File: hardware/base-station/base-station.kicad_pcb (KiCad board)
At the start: 4 copper layers, 30.3 x 90.5 mm, 123 parts, among them J2 USB4110GFA, J4 S3B-XH-A, J6 Conn_01x04, U1 W25Q64JVXGIQ TR, U12 MP2672AGD-0000-Z, U13 NTMD6N02R2G, U14 MAX17303G+, U15 479480001, U2 LM5157QRTERQ1, U22 TPS22918DBVR, U3 ESP32-S3RH2, U5 BQ21040DBVR, U9 TPS63021DSJR, Y1 ECS-.327-6-16R-TR, Y2 ECS-400-10-37B2-CKY-TR

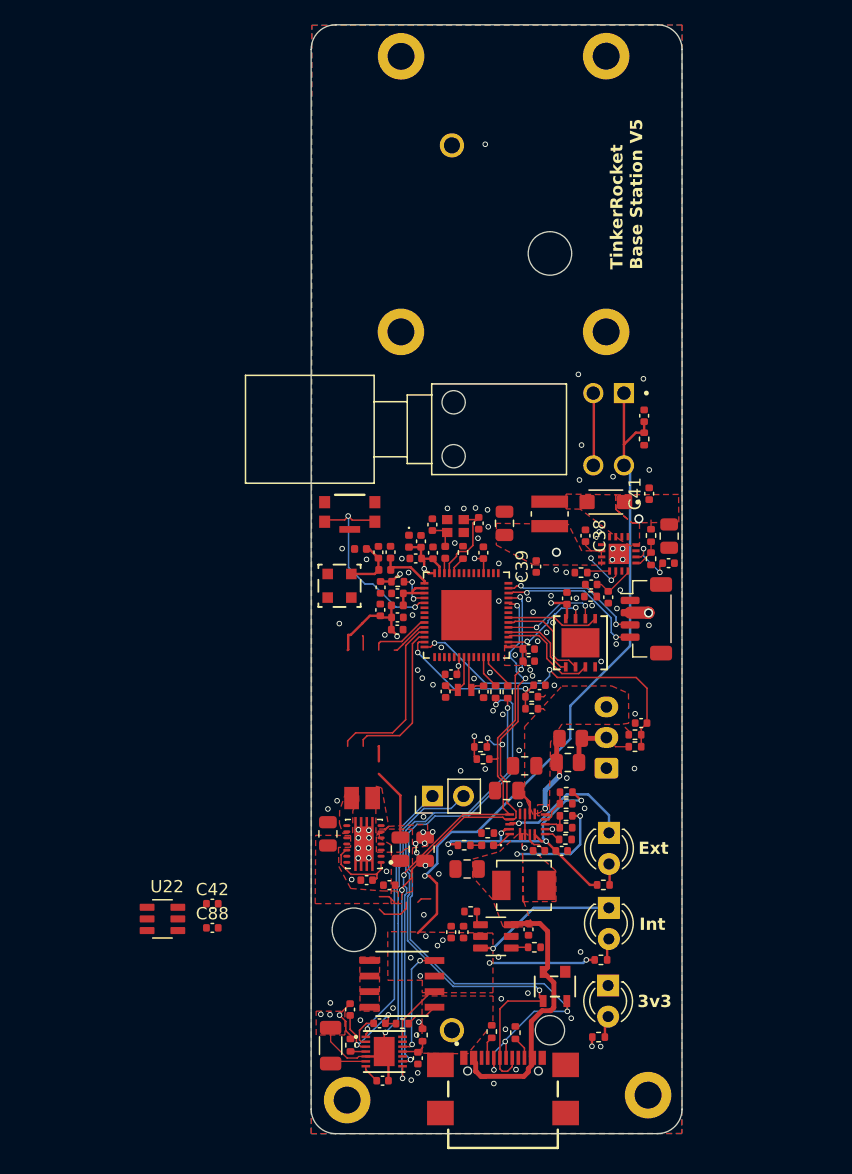
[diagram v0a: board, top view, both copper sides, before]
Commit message: hardware: battery protection, boost swap, and a capacitor voltage audit
Base station power chain, all verified against exported netlists:

- Protection: MAX17303G+ gauge/protector and its NTMD6N02R2G FET pair
  replaced by DW01A + 2x FS8205A. The MAX17303 had no firmware driver and
  the board never had a working coulomb counter, so state of charge already
  came from the voltage curve in bs_battery_soc.h; it now reads a 1M/1M
  divider on GPIO1. The FETs move from the positive rail to the negative
  one because the DW01A has no charge pump, so board ground is now P-,
  separated from the cell's B- by the FET stack. Two FS8205A in parallel
  put the 150 mV overcurrent trip at ~4.8-6.0 A instead of ~2.4-3.0 A.
  TH1 moves onto the BQ21040's TS pin, replacing a fixed 10k that had been
  defeating thermal charge cutoff.

- V_LORA retargeted 7.49 V -> 4.95 V and LM5157QRTERQ1 -> TPS61023DRLR.
  Nothing needed 7.4 V (everything downstream is 3.3 V behind the
  TPS62913), while an RFD868x-class radio is 5 V nominal with a 6 V
  absolute maximum, so the old rail put it permanently out of reach. Being
  synchronous and internally compensated also dropped D2, C35-C38 and R10.
  Inductor stays the fleet 2.2 uH: inside TI's 0.37-2.9 uH range and the
  only value meeting their ripple-under-40%-of-average guidance at load.

- Keystone 1043P holder -> MYOUNG BH-18650-A5BJ001-2D. Terminal pitch
  72.30 vs 72.22 mm, so the battery nets did not move; BT2 is rotated 180
  degrees because this part's positive end is mirrored.

Across all four boards:

- Every crystal was mis-loaded. 32.768 kHz parts saw ~9 pF against a 6 pF
  spec and the 40 MHz saw 12.5 pF against 10 pF, both pulling slow. Moved
  to Seiko SC-32S (12.5 pF) with 22 pF load caps, and the 40 MHz caps to
  18 pF. The tolerance being paid for had been swamped several times over.

- Capacitor voltage audit, new Min V rating column in the BOM. Three parts
  were operating outside their rating on 8.4 V rails: 47 uF and 100 u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
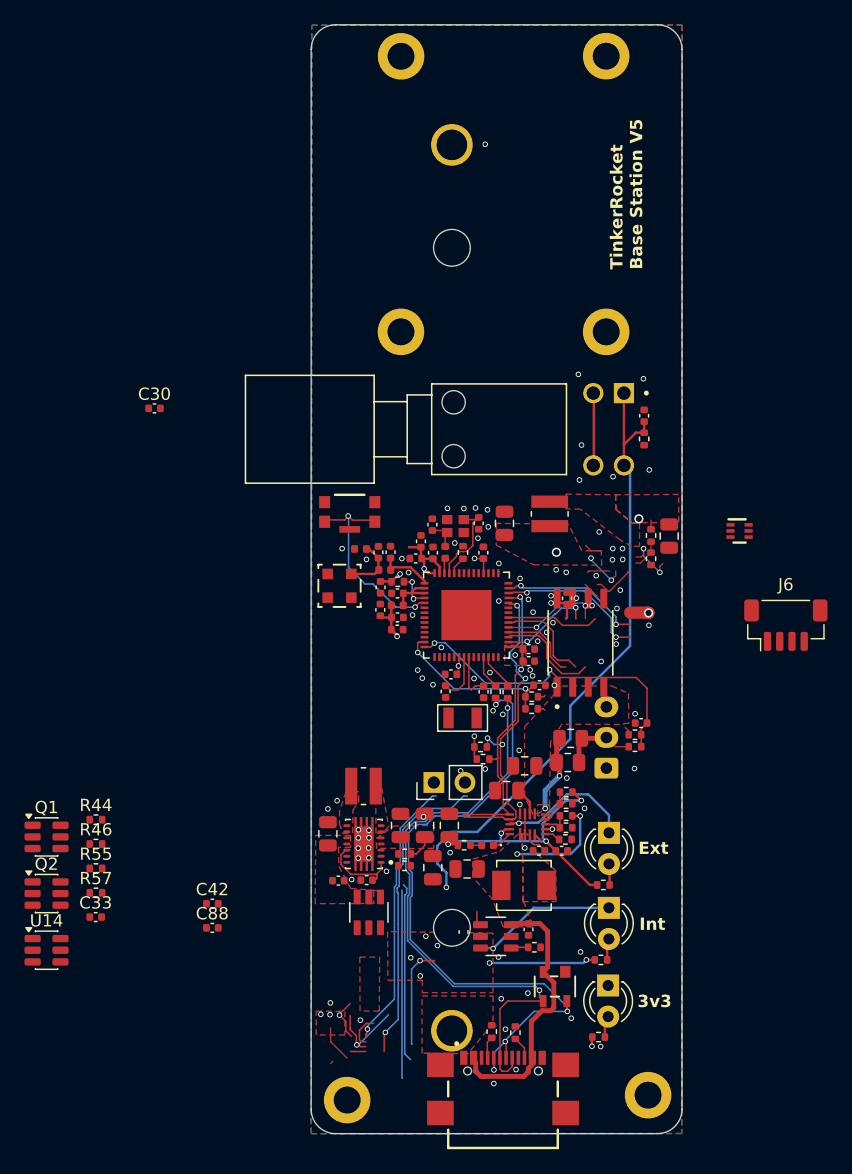
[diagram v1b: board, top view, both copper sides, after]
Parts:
- removed C20, C38: 1 uF, Capacitor_SMD:C_0402_1005Metric
- removed C31: 470 nF, Capacitor_SMD:C_0402_1005Metric
- removed C32, C39, C41: 100 nF, Capacitor_SMD:C_0402_1005Metric
- removed C35: 300 pF, Capacitor_SMD:C_0402_1005Metric
- removed C36: 15 nF, Capacitor_SMD:C_0402_1005Metric
- removed C37: 10 nF, Capacitor_SMD:C_0402_1005Metric
- removed D1: D_TVS, Diode_SMD:D_0402_1005Metric
- removed D2: SS24FL, Footprints:SODFL3617X108N
- removed L5: DFE201610E-1R0M=P2, Footprints:INDC2016X100N
- removed R10, R53: 10 k, Resistor_SMD:R_0402_1005Metric
- removed R18: 10 m, Resistor_SMD:R_1206_3216Metric
- removed the R40 at (61.8, 169.6)
- removed R56: 10, Resistor_SMD:R_0402_1005Metric
- removed R9: 442, Resistor_SMD:R_0402_1005Metric
- removed U13: NTMD6N02R2G, Footprints:SOIC8_4X5_ONS
- added C61: 22 uF, Capacitor_SMD:C_0805_2012Metric, F.Cu at (58.7, 169.0)
- added C62: 22 uF, Capacitor_SMD:C_0805_2012Metric, F.Cu at (57.3, 172.4)
- added L9: VLS3012CX-2R2M-1, Footprints:IND_VLS3012CX-2R2M-1, F.Cu at (51.7, 165.8)
- added Q1: FS8205A, Package_TO_SOT_SMD:SOT-23-6, F.Cu at (25.8, 169.9)
- added Q2: FS8205A, Package_TO_SOT_SMD:SOT-23-6, F.Cu at (25.8, 174.5)
- added R13: 1 M, Resistor_SMD:R_0402_1005Metric, F.Cu at (55.0, 171.3)
- added R16: 180 k, Resistor_SMD:R_0402_1005Metric, F.Cu at (55.0, 172.3)
- added R44: 1 M, Resistor_SMD:R_0402_1005Metric, F.Cu at (29.8, 168.5)
- added R46: 1 M, Resistor_SMD:R_0402_1005Metric, F.Cu at (29.8, 170.5)
- BT2: value 1043P -> BH-18650-A5BJ001-2D; footprint Footprints:BAT_1043P -> Footprints:BAT_BH-18650-A5BJ001-2D
- C2, C4: value 15 pF -> 22 pF
- C3, C6: value 22 pF -> 18 pF
- R11: value 100 k -> 732 k
- R12: value 15.4 k -> 100 k
- R57: value 1 k -> 2 k
- U1: value W25Q64JVXGIQ TR -> W25Q128JVSIQ; footprint Footprints:DFN_XGIQ TR_WIN -> Footprints:SOIC-8_W25Q128JVSIQ
- U14: value MAX17303G+ -> DW01A; footprint Footprints:21-0137I_T1433-2_MXM -> Package_TO_SOT_SMD:SOT-23-6
- U2: value LM5157QRTERQ1 -> TPS61023DRLR; footprint Footprints:RTE0016K -> Footprints:DRL0006A
- U9: value TPS63021DSJR -> TPS63020DSJR
- Y1: value ECS-.327-6-16R-TR -> SC-32S-32.768kHz-12.5pF; footprint Footprints:XTAL_ECS-.327-6-16R-TR -> Footprints:XTAL_SC-32S_3215
- moved C30 57.2 mm to (34.6, 134.9), turned to 0 degrees
- moved R55 29.9 mm to (29.8, 172.5), turned to 0 degrees
- moved U14 28.8 mm to (25.8, 179.2)
- moved R57 24.2 mm to (29.8, 174.5), turned to 0 degrees
- moved C33 22.1 mm to (29.8, 176.5), turned to 0 degrees
- moved U22 16.9 mm to (52.1, 176.1), turned to 90 degrees
- moved J6 11.4 mm to (86.1, 152.6), turned to 0 degrees
- moved U2 10.0 mm to (82.4, 145.0)
- moved C23 4.18 mm to (49.6, 173.5), turned to 0 degrees
- moved Y1 2.29 mm to (59.8, 160.2)
- moved C60 1.93 mm to (56.7, 169.0), turned to 90 degrees
- moved C58 1.93 mm to (54.7, 169.0), turned to 90 degrees
- moved TH1 1.12 mm to (57.4, 165.5)
- turned BT2 to 90 degrees
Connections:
- net Vcc renamed CHG_VCC
- BT2 pad N: Net-(U14-CSP) -> /Battery/B-
- BT2 pad P: Net-(U13-SOURCE1) -> VCC
- C30 pad 1: Net-(U14-PCKP) -> Volt_Read
- C33 pad 1: Net-(U14-BATT) -> Net-(U14-VCC)
- C33 pad 2: Net-(U14-CSP) -> /Battery/B-
- L8 pad 2: Net-(D2-PadA) -> Net-(U2-SW)
- R55 pad 2: Net-(U14-PCKP) -> Net-(U14-VCC)
- R57 pad 1: Net-(U14-CSP) -> Net-(U14-VM)
- R57 pad 2: Net-(U14-PFAIL) -> GND
- TH1 pad 1: Net-(U14-TH) -> Net-(U5-TS)
- TH1 pad 2: Net-(U14-CSP) -> GND
- U14 pad 1: Net-(U14-TH) -> Net-(Q1-G1)
- U14 pad 2: Net-(U14-CP) -> Net-(U14-VM)
- U14 pad 3: Net-(U14-BATT) -> Net-(Q1-G2)
- U14 pad 4: Net-(U14-PFAIL) -> unconnected-(U14-TD-Pad4)
- U14 pad 5: Net-(U14-CSP) -> Net-(U14-VCC)
- U14 pad 6: GND -> /Battery/B-
- U2 pad 1: GND -> Net-(U2-FB)
- U2 pad 2: Net-(U2-VCC) -> VCC
- U2 pad 4: unconnected-(U2-PGOOD-Pad4) -> GND
- U2 pad 5: Net-(U2-RT) -> Net-(U2-SW)
- U2 pad 6: VCC -> V_LORA
- U3 pad 38: SDA_SENS -> unconnected-(U3-GPIO33-Pad38)
- U3 pad 39: SCL_SENS -> unconnected-(U3-GPIO34-Pad39)
- U3 pad 6: unconnected-(U3-GPIO1-Pad6) -> Volt_Read
- U9 pad 3: +3V3 -> Net-(U9-FB)
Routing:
- net GND: track 4.33 -> 48.7 mm, vias 102 -> 95
- net Net-(U14-CSP): track 37.4 -> 0.00 mm, vias 4 -> 0
- net SDA_SENS: track 51.5 -> 27.2 mm, vias 6 -> 4
- net SCL_SENS: track 47.8 -> 24.7 mm, vias 4 -> 2
- net Net-(U14-TH): track 22.2 -> 0.00 mm, vias 1 -> 0
- net Net-(U5-TS): track 1.20 -> 23.4 mm, vias 0 -> 1
- net (no net): track 5.66 -> 27.3 mm, vias 0 -> 4
- net Net-(U9-FB): track 0.00 -> 14.6 mm
- net M_FLASH_CS: track 13.9 -> 0.00 mm
- net M_MISO: track 12.8 -> 0.00 mm
- net Net-(U13-GATE2): track 9.19 -> 0.00 mm, vias 2 -> 0
- net Net-(U14-BATT): track 8.72 -> 0.00 mm, vias 2 -> 0
- net +3V3: track 28.3 -> 19.9 mm, vias 10 -> 7
- net Net-(U22-ON): track 57.2 -> 52.1 mm
- net M_SCK: track 4.99 -> 0.00 mm
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- added copper zone on F.Cu, net (none)
- added copper zone on In2.Cu, net /Battery/B-
- added copper zone on F.Cu, net Net-(U2-SW)
- removed copper zone on F.Cu, net Net-(D2-PadA)
- removed copper zone on F.Cu, net Net-(U13-DRAIN1-Pad7)
- removed copper zone on F.Cu, net Net-(U13-SOURCE1)
- removed copper zone on F.Cu, net Net-(U14-CSP)
- removed copper zone on In2.Cu, net Net-(U14-CSP)

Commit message: hardware: place Q3 and bump C10 to 10 uF on the base-station
Places the third FS8205A whose schematic went in with the previous
commit, so the protection stack is now Q1/Q2/Q3 on the board as well as
on the sheet.

C10 goes 1 uF -> 10 uF. Changed in both esp32_p3.kicad_sch and the
layout, so schematic and board agree.

The battery sheet is rewired - +9 wires, +3 junctions, -5 labels - with
no change to its part set.

Layout otherwise: 38 parts repositioned, 24 track segments removed, 35
vias added, one zone removed.

Co-Authored-By: Claude Opus 5 <noreply@anthropic.com>
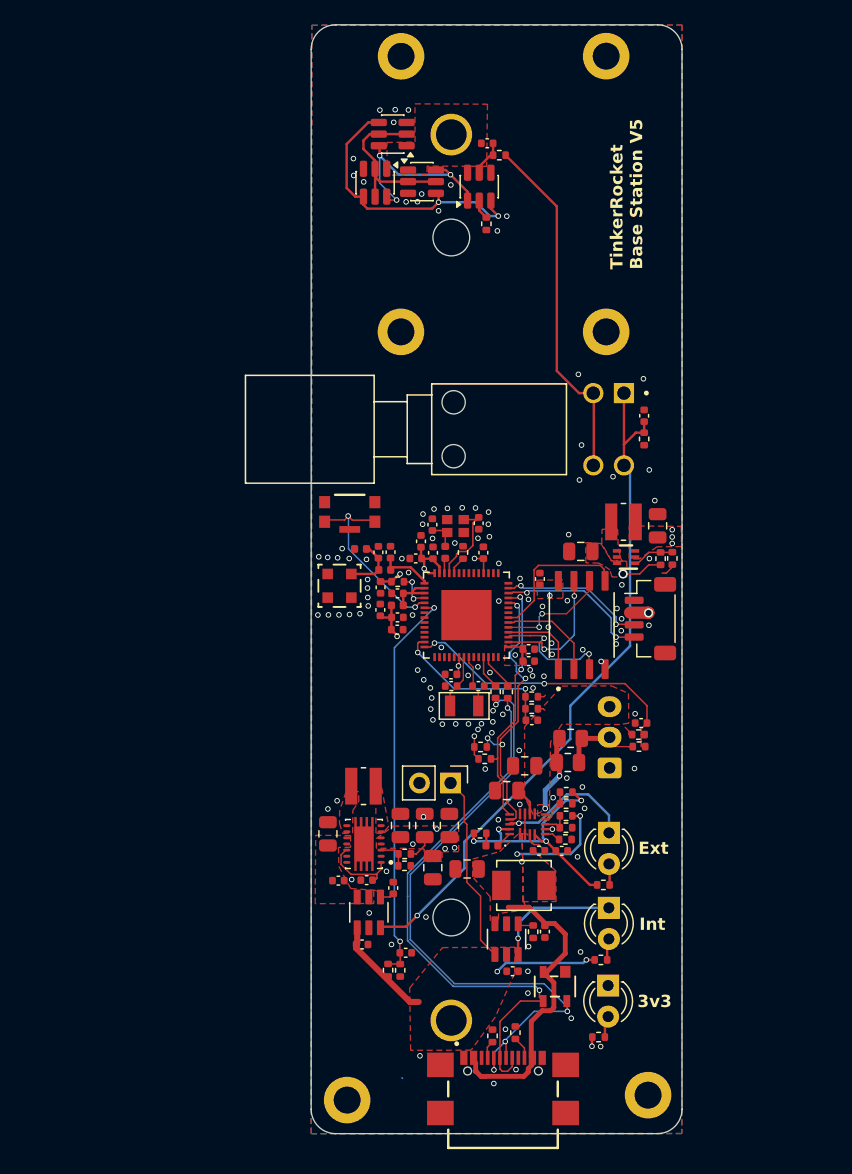
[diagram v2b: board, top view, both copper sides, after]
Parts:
- added Q3: FS8205A, Package_TO_SOT_SMD:SOT-23-6, F.Cu at (52.6, 116.5)
- C10: value 1 uF -> 10 uF
- R55: value 1 k -> 100
- moved U14 71.6 mm to (61.1, 116.8), turned to 90 degrees
- moved C33 70.8 mm to (61.8, 113.3), turned to 180 degrees
- moved Q2 68.1 mm to (54.1, 112.6), turned to 180 degrees
- moved R55 66.9 mm to (62.8, 114.3), turned to 180 degrees
- moved R57 63.2 mm to (61.7, 119.9), turned to -90 degrees
- moved Q1 61.6 mm to (56.4, 116.4)
- moved C30 48.9 mm to (55.1, 179.4)
- moved R46 26.9 mm to (54.7, 180.8), turned to -90 degrees
- moved R44 26.8 mm to (53.7, 180.8), turned to 90 degrees
- moved C88 15.1 mm to (54.1, 174.1), turned to 90 degrees
- moved C42 12.7 mm to (51.6, 178.7)
- moved C34 12.5 mm to (75.7, 144.5)
- moved J6 11.1 mm to (75.1, 152.1), turned to -90 degrees
- moved U2 9.51 mm to (73.1, 147.1), turned to 180 degrees
- moved C40 7.32 mm to (69.4, 146.6), turned to 180 degrees
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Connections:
- net Net-(Q1-D1/D2-Pad2) renamed /Battery/PROT_DRAIN
- U3 pad 38: unconnected-(U3-GPIO33-Pad38) -> SDA_SENS
- U3 pad 39: unconnected-(U3-GPIO34-Pad39) -> SCL_SENS
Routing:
- net GND: track 48.7 -> 2.69 mm, vias 95 -> 125
- net Volt_Read: track 0.00 -> 32.4 mm, vias 0 -> 2
- net (no net): track 27.3 -> 0.00 mm, vias 4 -> 0
- net Net-(Q1-G2): track 0.00 -> 23.4 mm, vias 0 -> 2
- net VCC: track 89.9 -> 112.5 mm, vias 8 -> 5
- net Net-(Q1-G1): track 0.00 -> 16.4 mm, vias 0 -> 3
- net /Battery/PROT_DRAIN: track 0.00 -> 14.5 mm
- net Net-(U9-FB): track 14.6 -> 2.66 mm
- net Net-(U5-TS): track 23.4 -> 15.5 mm, vias 1 -> 0
- net Net-(U22-ON): track 52.1 -> 57.1 mm
- net SDA_SENS: track 27.2 -> 23.4 mm
- net SCL_SENS: track 24.7 -> 20.9 mm
- net SPI_HD: track 7.67 -> 10.7 mm
- net Net-(U14-VCC): track 0.00 -> 3.02 mm
- net VBUS: track 30.4 -> 33.2 mm
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- added copper zone on F.Cu, net /Battery/B-
- removed copper zone on F.Cu, net (none)
- removed copper zone on In2.Cu, net /Battery/B-

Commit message: hardware: single-source each board's version through the title block
Every board hardcoded its marketing version inside a silkscreen gr_text
("LoRa V3", "Tinker\nRocket\nV9", ...), where it could drift from the git
tag with nothing to catch it.

The version token now lives in the PCB title block as (rev "V3") and the
silkscreen references ${REVISION}. KiCad resolves that at plot time,
including from kicad-cli, so the artwork is unchanged -- verified by
plotting F.SilkS + B.SilkS for all five boards before and after and
comparing stroke counts:

  lora-daughterboard      260 -> 260
  rocket-computer        1236 -> 1236
  base-station            687 -> 687
  gnss-sam10m8-18mm-hv    366 -> 366
  gnss-px1105r-...        353 -> 353

Four changed lines per board and nothing else. servo-adapter is untouched
-- it carries no version on silkscreen yet.

Co-Authored-By: Claude Opus 5 <noreply@anthropic.com>
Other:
- board text added: "TinkerRocket Base Station ${REVISION}"
- board text removed: "TinkerRocket Base Station V5"
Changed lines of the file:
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@@
 	)
 	(paper "A4")
+	(title_block
+		(rev "V5")
+	)
 	(layers
 		(0 "F.Cu" signal)
@@
 		)
 	)
-	(gr_text "TinkerRocket\nBase Station V5"
+	(gr_text "TinkerRocket\nBase Station ${REVISION}"
 		(at 74.54 123.61 90)
 		(layer "F.SilkS")

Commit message: hardware: declare filled+capped vias on the 6-layer boards; in-progress board edits
Two separate things, kept together because they land in the same board files.

1. Via protection, mine.  lora-daughterboard and rocket-computer both place
   vias in pads, and the fab fills those on 6-layer stackups -- but the board
   files still declared (filling no) (capping no), so nothing in the exported
   data said so.  Both now declare IPC-4761 Type VII (filled and capped),
   which is the process via-in-pad actually requires.  base-station is left at
   (filling no) (capping no): it is 4-layer and does not get the treatment.

2. In-progress layout work, the user's, carried along in the same files:

   rocket-computer  J7 removed (superseded by the J8 JST VH battery inlet);
                    C20/C22/C48/C49 crystal caps 18 pF -> 12 pF now reflected
                    in copper; 8 parts flipped side, 23 repositioned, routing
                    and via count adjusted to suit
   lora-daughterboard  routing and ground stitching (+8 vias, +10 segments)
   base-station     one via removed
   gnss-sam10m8-18mm-hv       C15 added; C11/C13 47 uF -> 22 uF
   gnss-px1105r-...-ext-ant   C16/R8/R9 added; C13/C14 47 uF -> 22 uF

The 47 -> 22 uF swap on both GNSS boards is already reflected in the
cross-board BOM: the 47 uF line is now rocket-computer only (1), and 22 uF
GNSS went 5 -> 8.

Co-Authored-By: Claude Opus 5 <noreply@anthropic.com>
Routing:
- net GND: vias 125 -> 124
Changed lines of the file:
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@@
 	)
 	(via
-		(at 56.57 168.28)
-		(size 0.45)
-		(drill 0.3)
-		(layers "F.Cu" "B.Cu")
-		(free yes)
-		(net "GND")
-	)
-	(via
 		(at 72.76 149.35)
 		(size 0.45)
@@
 	)
 	(segment
+		(start 51.67 113.08)
+		(end 52.19 112.56)
+		(width 0.2)
+		(layer "F.Cu")
+		(net "/Battery/PROT_DRAIN")
+	)
+	(segment
+		(start 54.37 112.56)
+		(end 55.195 112.56)
+		(width 0.2)
+		(layer "F.Cu")
+		(net "/Battery/PROT_DRAIN")
+	)
+	(segment
+		(start 52.62 114.727501)
+		(end 51.67 113.777501)
+		(width 0.2)
+		(layer "F.Cu")
+		(net "/Battery/PROT_DRAIN")
+	)
+	(segment
+		(start 53.007501 116.44)
+		(end 52.62 116.052499)
+		(width 0.2)
+		(layer "F.Cu")
+		(net "/Battery/PROT_DRAIN")
+	)
+	(segment
+		(start 54.37 112.56)
+		(end 52.92 112.56)
+		(width 0.2)
+		(layer "F.Cu")
+		(net "/Battery/PROT_DRAIN")
+	)
+	(segment
+		(start 52.62 115.39)
+		(end 52.62 114.727501)
+		(width 0.2)
+		(layer "F.Cu")
+		(net "/Battery/PROT_DRAIN")
+	)
+	(segment
+		(start 52.62 115.39)
+		(end 52.62 117.665)
+		(width 0.2)
+		(layer "F.Cu")
+		(net "/Battery/PROT_DRAIN")
+	)
+	(segment
+		(start 51.67 113.777501)
+		(end 51.67 113.08)
+		(width 0.2)
+		(layer "F.Cu")
+		(net "/Battery/PROT_DRAIN")
+	)
+	(segment
+		(start 52.19 112.56)
+		(end 52.92 112.56)
+		(width 0.2)
+		(layer "F.Cu")
+		(net "/Battery/PROT_DRAIN")
+	)
+	(segment
+		(start 52.62 116.052499)
+		(end 52.62 115.39)
+		(width 0.2)
+		(layer "F.Cu")
+		(net "/Battery/PROT_DRAIN")
+	)
+	(segment
+		(start 57.585 116.44)
+		(end 55.31 116.44)
+		(width 0.2)
+		(layer "F.Cu")
+		(net "/Battery/PROT_DRAIN")
+	)
+	(segment
+		(start 55.31 116.44)
+		(end 53.007501 116.44)
+		(width 0.2)
+		(layer "F.Cu")
+		(net "/Battery/PROT_DRAIN")
+	)
+	(segment
 		(start 51.98646 118.643959)
 		(end 57.276041 118.643959)
@@
 		(net "Net-(U5-ISET)")
 	)
-	(segment
-		(start 51.67 113.08)
-		(end 52.19 112.56)
-		(width 0.2)
-		(layer "F.Cu")
-		(net "/Battery/PROT_DRAIN")
-	)
-	(segment
-		(start 54.37 112.56)
-		(end 55.195 112.56)
-		(width 0.2)
-		(layer "F.Cu")
-		(net "/Battery/PROT_DRAIN")
-	)
-	(segment
-		(start 52.62 114.727501)
-		(end 51.67 113.777501)
-		(width 0.2)
-		(layer "F.Cu")
-		(net "/Battery/PROT_DRAIN")
-	)
-	(segment
-		(start 53.007501 116.44)
-		(end 52.62 116.052499)
-		(width 0.2)
-		(layer "F.Cu")
-		(net "/Battery/PROT_DRAIN")
-	)
-	(segment
-		(start 54.37 112.56)
-		(end 52.92 112.56)
-		(width 0.2)
-		(layer "F.Cu")
-		(net "/Battery/PROT_DRAIN")
-	)
-	(segment
-		(start 52.62 115.39)
-		(end 52.62 114.727501)
-		(width 0.2)
-		(layer "F.Cu")
-		(net "/Battery/PROT_DRAIN")
-	)
-	(segment
-		(start 52.62 115.39)
-		(end 52.62 117.665)
-		(width 0.2)
-		(layer "F.Cu")
-		(net "/Battery/PROT_DRAIN")
-	)
-	(segment
-		(start 51.67 113.777501)
-		(end 51.67 113.08)
-		(width 0.2)
-		(layer "F.Cu")
-		(net "/Battery/PROT_DRAIN")
-	)
-	(segment
-		(start 52.19 112.56)
-		(end 52.92 112.56)
-		(width 0.2)
-		(layer "F.Cu")
-		(net "/Battery/PROT_DRAIN")
-	)
-	(segment
-		(start 52.62 116.052499)
-		(end 52.62 115.39)
-		(width 0.2)
-		(layer "F.Cu")
-		(net "/Battery/PROT_DRAIN")
-	)
-	(segment
-		(start 57.585 116.44)
-		(end 55.31 116.44)
-		(width 0.2)
-		(layer "F.Cu")
-		(net "/Battery/PROT_DRAIN")
-	)
-	(segment
-		(start 55.31 116.44)
-		(end 53.007501 116.44)
-		(width 0.2)
-		(layer "F.Cu")
-		(net "/Battery/PROT_DRAIN")
-	)
 	(zone
